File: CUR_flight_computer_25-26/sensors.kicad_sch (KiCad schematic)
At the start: 0 parts

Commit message: Baro schematic
Hooked up 4-wire SPI
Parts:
- added C1: 100n, symbol Device:C_Small
- added C2: 4.7u, symbol Device:C_Small
- added U2: LPS22HB, Package_LGA:ST_HLGA-10_2x2mm_P0.5mm_LayoutBorder3x2y, symbol Sensor_Pressure:LPS22HB
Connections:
- new net +3V3: C1.1, C2.1, U2.1 (Vdd_IO), U2.10 (VDD)
- new net BARO_CS: U2.6 (~{CS})
- new net BARO_INT: U2.7 (INT_DRDY)
- new net GND: C1.2, C2.2, U2.3 (GND), U2.8 (GND), U2.9 (GND)
- new net SENSOR_MISO: U2.5 (SA0)
- new net SENSOR_MOSI: U2.4 (SDA)
- new net SENSOR_SPC: U2.2 (SCL)

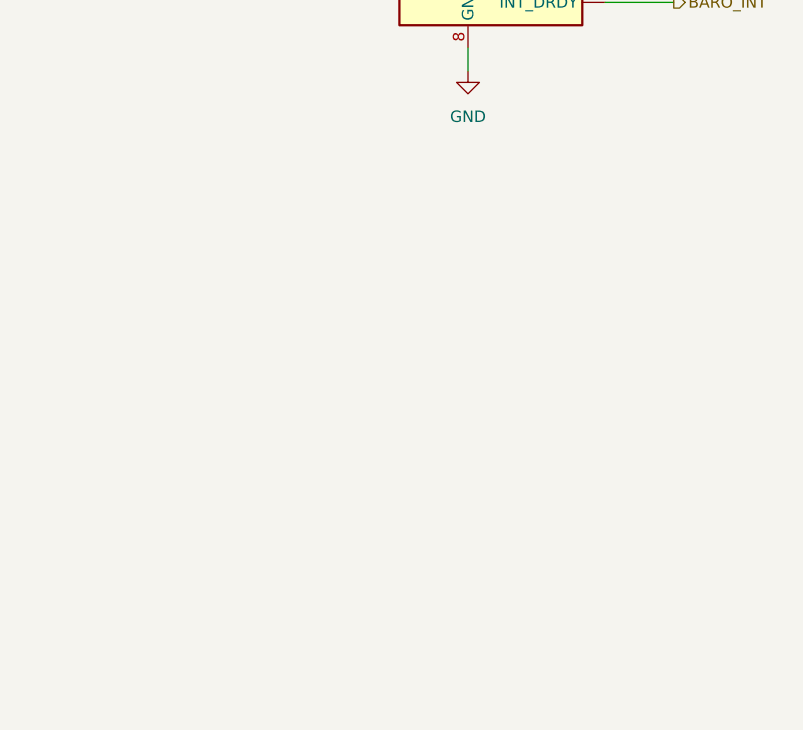
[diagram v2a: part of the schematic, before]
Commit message: added mag
copy pasted magnometer schematic
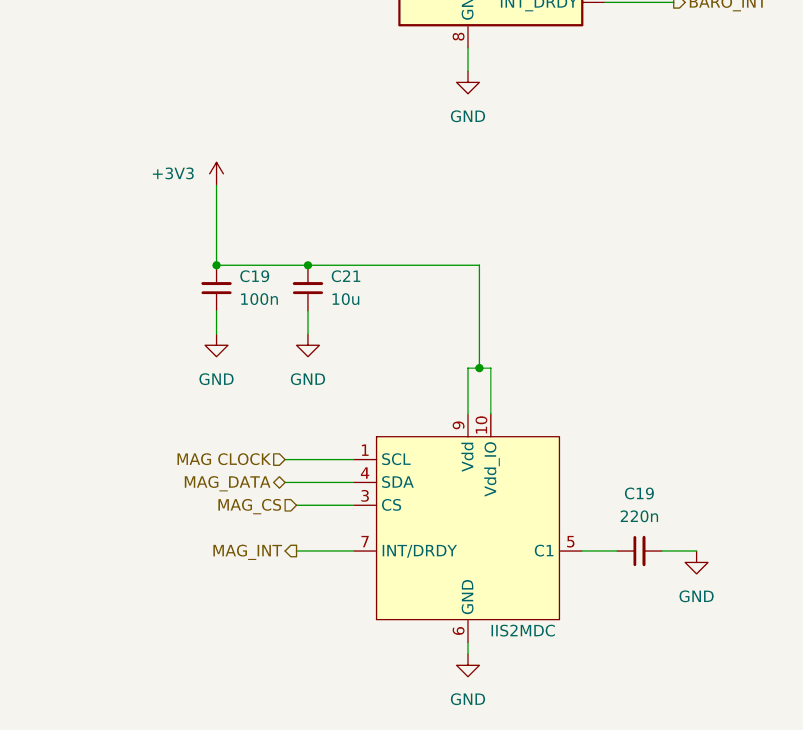
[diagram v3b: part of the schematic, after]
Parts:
- added C19: 220n, symbol Device:C_Small
- added C19: 100n, symbol Device:C_Small
- added C21: 10u, symbol Device:C_Small
- added U6: IIS2MDC, ST_IIS2MDC:LGA-12_2X2X0P7_STM, symbol ST_Sensor_IMU:IIS2MDC
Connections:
- net +3V3: now also C19.2, C21.2, U6.10 (Vdd_IO), U6.9 (Vdd)
- net GND: now also C19.1, C19.2, C21.1, U6.6 (GND), U6.8 (GND)
- new net: C19.1, U6.5 (C1)
- new net: U6.11 (NC), U6.12 (NC), U6.2 (NC)
- new net MAG CLOCK: U6.1 (SCL)
- new net MAG_CS: U6.3 (CS)
- new net MAG_DATA: U6.4 (SDA)
- new net MAG_INT: U6.7 (INT/DRDY)

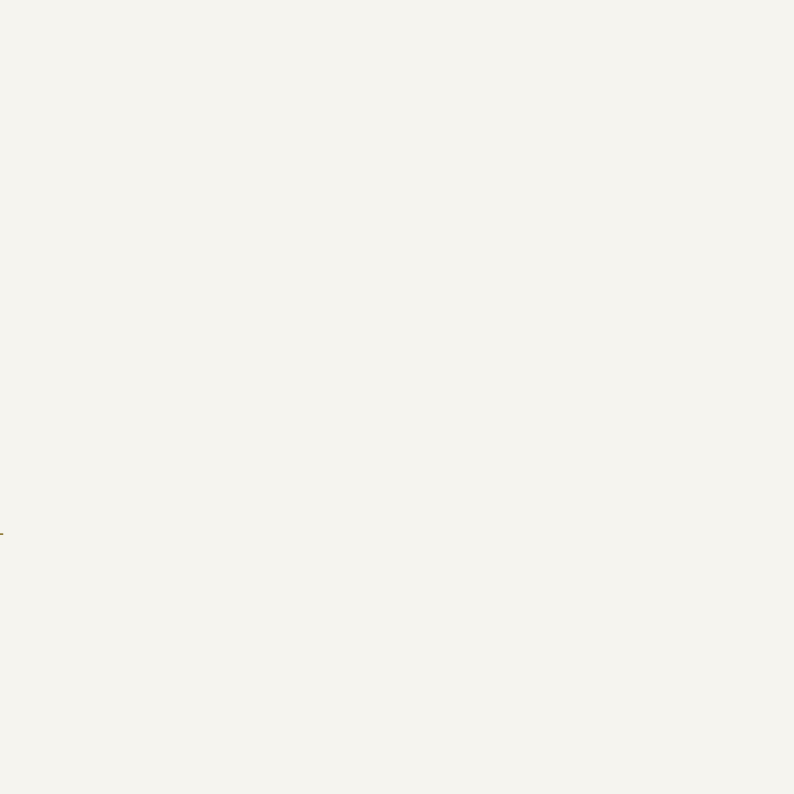
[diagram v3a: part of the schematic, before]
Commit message: Update sensors.kicad_sch
fixed imu issues by copying imu from correct branch...
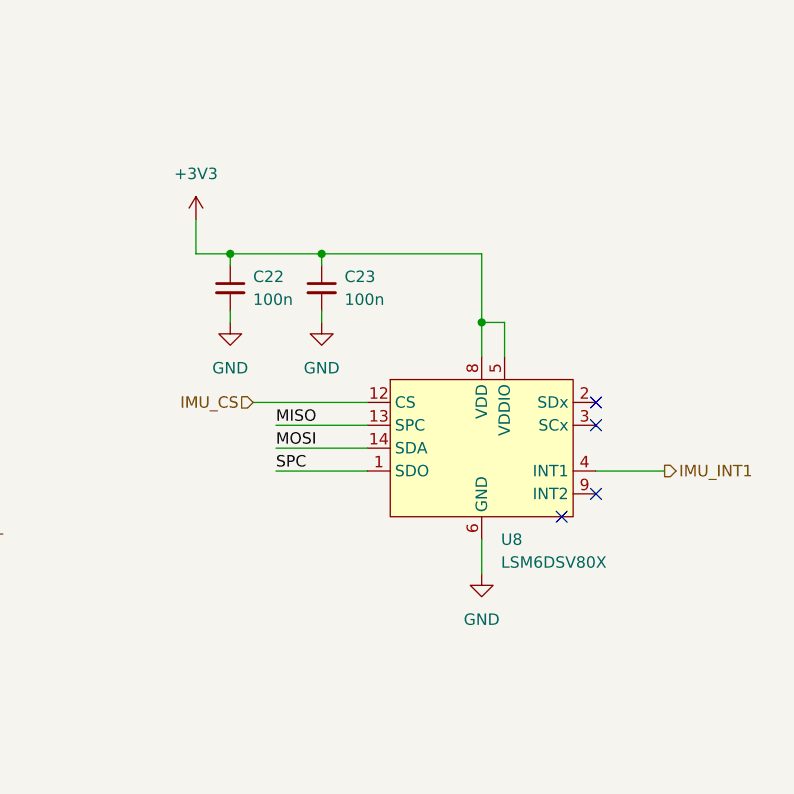
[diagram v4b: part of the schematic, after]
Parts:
- added C22, C23: 100n, symbol Device:C_Small
- added U8: LSM6DSV80X, Package_LGA:LGA-14_3x2.5mm_P0.5mm_LayoutBorder3x4y, symbol ST_Sensor_IMU:LSM6DSV80X
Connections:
- net +3V3: now also C22.1, C23.1, U8.5 (VDDIO), U8.8 (VDD)
- net GND: now also C22.2, C23.2, U8.6 (GND), U8.7 (GND)
- net SENSOR_MISO: now also U8.13 (SCL)
- net SENSOR_MOSI: now also U8.14 (SDA)
- net SENSOR_SPC: now also U8.1 (SDO)
- new net: U8.10 (NC), U8.11 (NC)
- new net IMU_CS: U8.12 (CS)
- new net IMU_INT1: U8.4 (INT1)
- no-connect marks 0 -> 4

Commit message: updated pins
updated all sensor pins
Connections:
- net IMU_INT2: now reaches U8.9 (INT2)
- no-connect marks 4 -> 3
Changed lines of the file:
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@@
-	)
-	(no_connect
-		(at 165.1 78.74)
 	)
 	(no_connect
@@
 		(pts
 			(xy 45.72 134.62) (xy 53.34 134.62)
+		)
+		(stroke
+			(width 0)
+			(type default)
+		)
+	)
+	(wire
+		(pts
+			(xy 165.1 78.74) (xy 172.72 78.74)
 		)
 		(stroke
@@
 		(effects
 			(font
+				(size 1.27 1.27)
+			)
+			(justify left)
+		)
+	)
+	(hierarchical_label "IMU_INT2"
+		(shape output)
+		(at 172.72 78.74 0)
+		(effects
+			(font

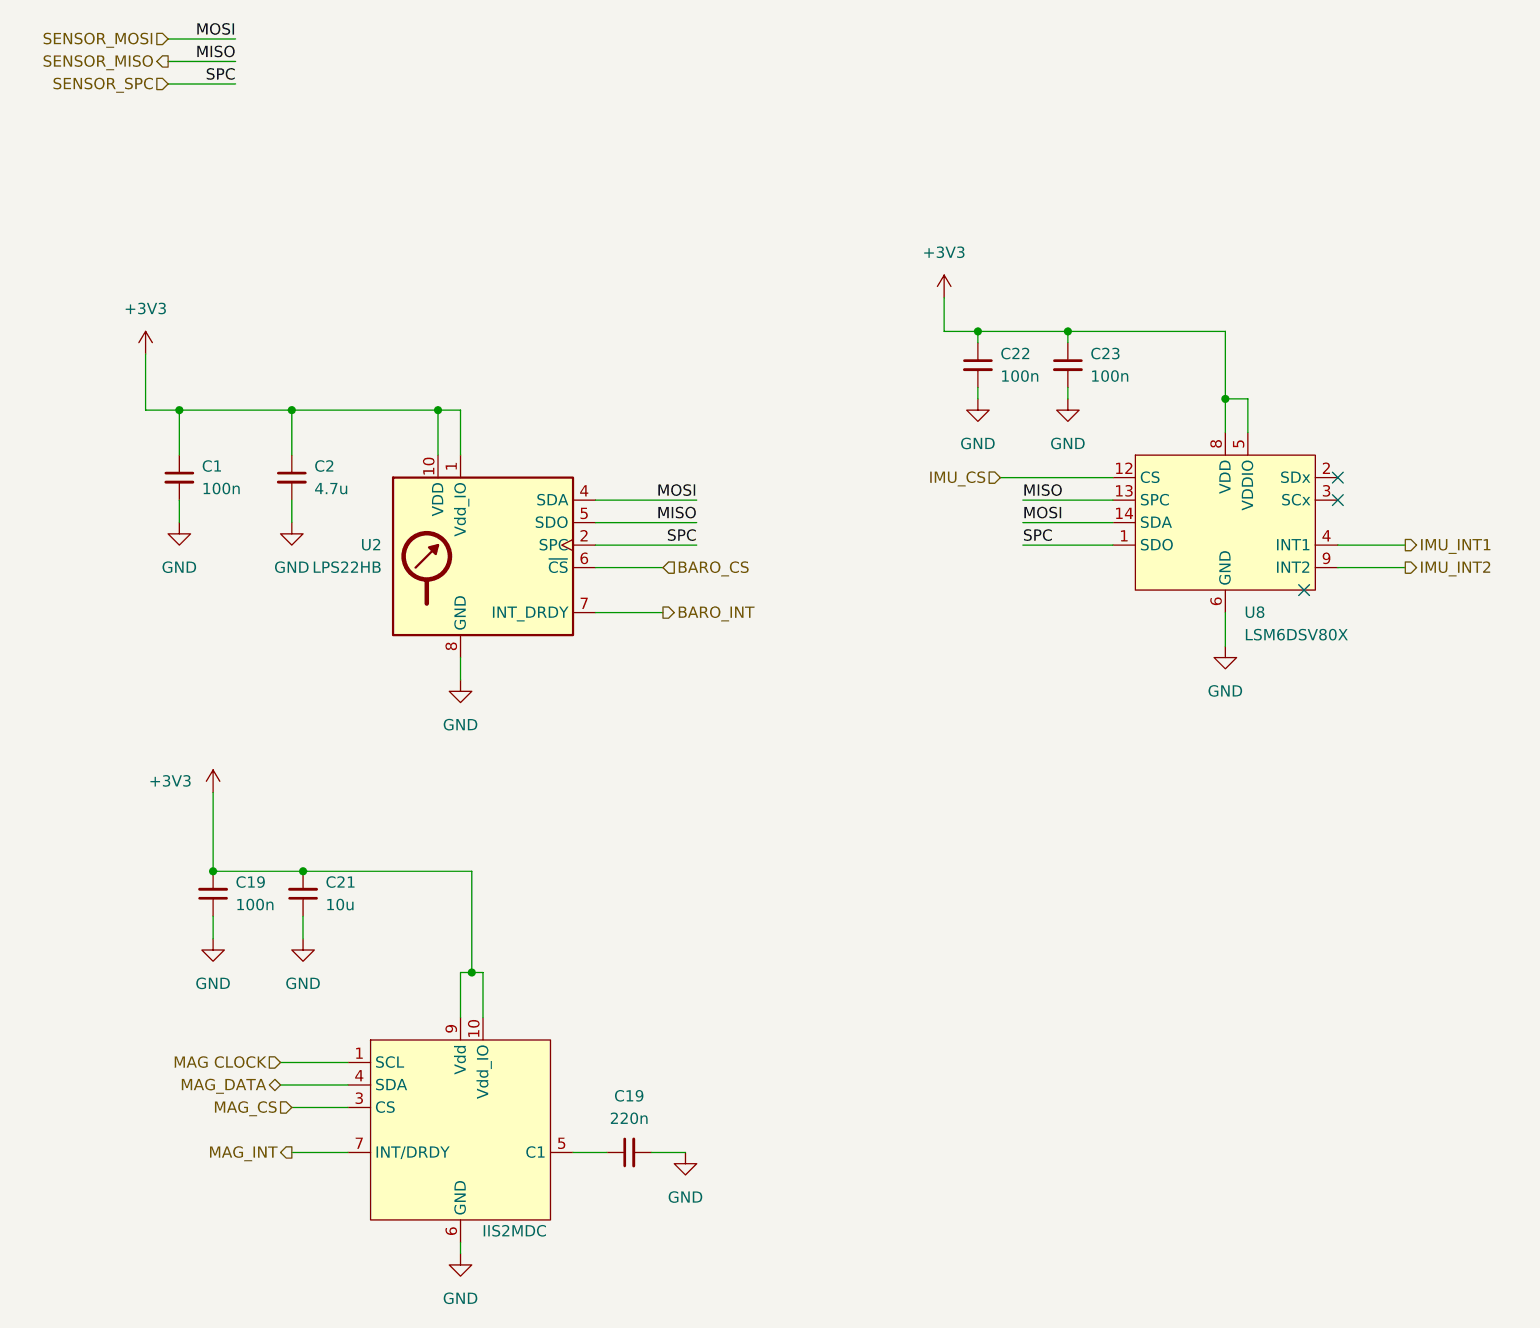
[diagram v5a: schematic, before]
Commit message: hooked up more pins
added lcd header as well
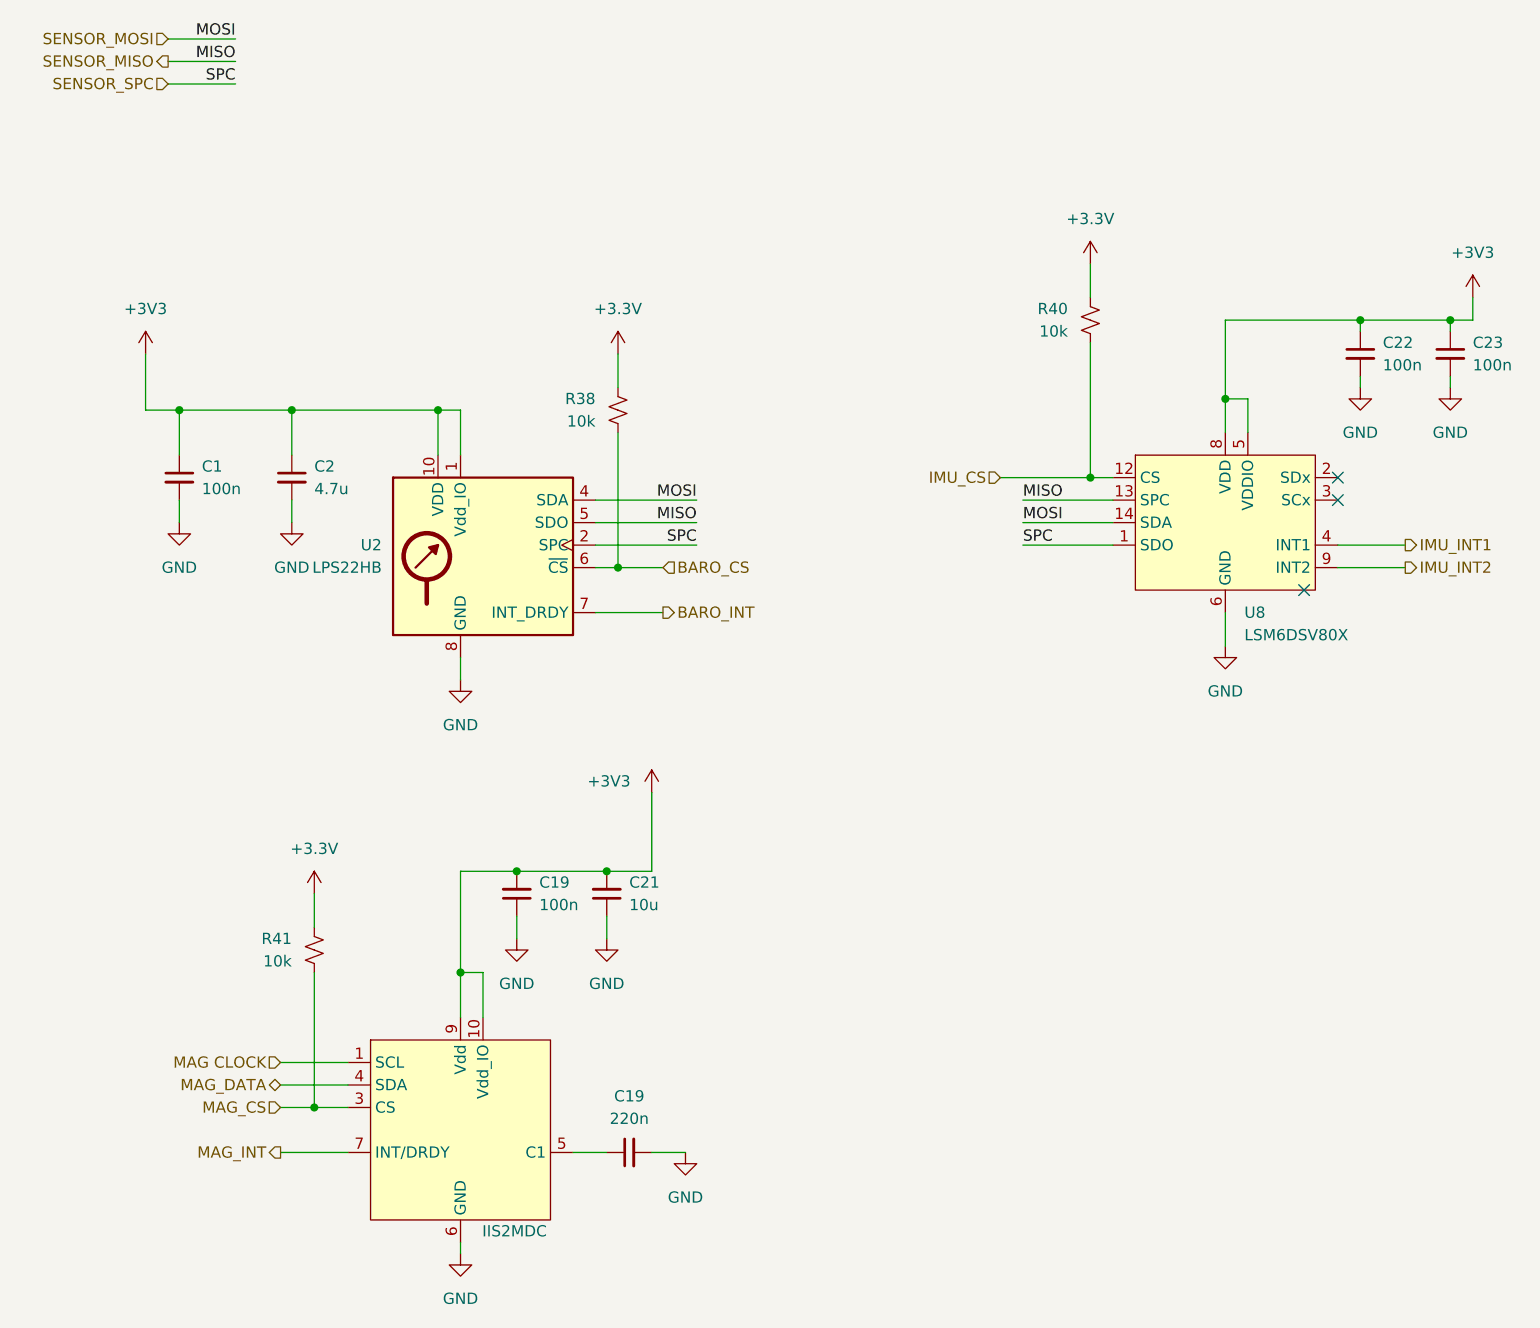
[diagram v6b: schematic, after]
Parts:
- added R38, R40, R41: 10k, symbol Device:R_Small_US
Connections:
- net BARO_CS: now also R38.2
- net IMU_CS: now also R40.2
- net MAG_CS: now also R41.2
- new net +3.3V: R38.1, R40.1, R41.1
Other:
- moved on the sheet: C19, C21, C22, C23
